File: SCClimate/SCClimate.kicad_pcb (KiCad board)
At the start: 2 copper layers, 100.5 x 54.9 mm, 77 parts, among them J11 HVAC, J3 DISP_SERIAL, J4 SERIAL, J7 PIR, Q1 TEPT5700, Q6 2N6073B, Q7 2N6073B, Q8 2N6073B, SW1 RESET, SW2 MODE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

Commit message: Changed a few things around for better placement
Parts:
- removed SW3: 1825232-1, footprints:1825232-1
- added Q2: 2N7002, digikey-footprints:SOT-23-3, F.Cu at (132.1, 121.9)
- added R3: 10K, Resistor_SMD:R_0805_2012Metric_Pad1.20x1.40mm_HandSolder, F.Cu at (93.3, 92.2)
- added R4: 10K, Resistor_SMD:R_0805_2012Metric_Pad1.20x1.40mm_HandSolder, F.Cu at (128.0, 95.2)
- added R5: 10K, Resistor_SMD:R_0805_2012Metric_Pad1.20x1.40mm_HandSolder, F.Cu at (128.0, 92.3)
- C13, C21, C22, C3, U7: moved to B.Cu
- D2, D3, D4, R12, R15, R16, TRIAC_G1, TRIAC_W1, TRIAC_Y1: moved to F.Cu
- J7: footprint Connector_PinSocket_2.54mm:PinSocket_1x05_P2.54mm_Vertical -> Connector_PinSocket_2.54mm:PinSocket_1x03_P2.54mm_Vertical
- R9: value 20K -> 10K
- moved J11 15.5 mm to (43.1, 96.1), turned to 270 degrees
- moved C22 9.00 mm to (133.7, 95.6), turned to 0 degrees
- moved C21 5.84 mm to (133.7, 93.0), turned to 0 degrees
- moved U7 3.23 mm to (130.8, 87.6), turned to 270 degrees
- moved J7 2.54 mm to (128.7, 132.8)
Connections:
- J11 pad 1: /G_TERM -> /RC_TERM
- J11 pad 2: /RC_TERM -> /W_TERM
- J11 pad 4: /C_TERM -> /G_TERM
- J11 pad 5: /W_TERM -> /C_TERM
- J3 pad 4: +5V -> Net-(J3-Pad4)
- J4 pad 2: Net-(J4-Pad2) -> +3V3
- J4 pad 3: +3V3 -> (no net)
- J7 pad 1: Net-(J7-Pad1) -> GND
- J7 pad 2: GND -> /PIR
- J7 pad 3: /PIR -> +5V
- Q1 pad 1: +3V3 -> Net-(Q1-Pad1)
- U1 pad 10: /TRIAC_W -> /TRIAC_G
- U1 pad 11: Net-(U1-Pad11) -> /DISP_EN
- U1 pad 12: Net-(U1-Pad12) -> (no net)
- U1 pad 13: Net-(U1-Pad13) -> (no net)
- U1 pad 14: Net-(U1-Pad14) -> (no net)
- U1 pad 16: Net-(U1-Pad16) -> (no net)
- U1 pad 17: Net-(U1-Pad17) -> (no net)
- U1 pad 18: Net-(U1-Pad18) -> (no net)
- U1 pad 19: Net-(U1-Pad19) -> (no net)
- U1 pad 20: Net-(U1-Pad20) -> (no net)
- U1 pad 21: Net-(U1-Pad21) -> (no net)
- U1 pad 22: Net-(U1-Pad22) -> (no net)
- U1 pad 23: Net-(U1-Pad23) -> (no net)
- U1 pad 24: Net-(U1-Pad24) -> (no net)
- U1 pad 27: Net-(U1-Pad27) -> (no net)
- U1 pad 28: Net-(U1-Pad28) -> (no net)
- U1 pad 32: Net-(U1-Pad32) -> (no net)
- U1 pad 33: /ESP_GPIO26 -> (no net)
- U1 pad 36: /I2C_SDA -> /I2C_SCL
- U1 pad 37: /I2C_SCL -> /I2C_SDA
- U1 pad 4: Net-(U1-Pad4) -> (no net)
- U1 pad 5: Net-(U1-Pad5) -> (no net)
- U1 pad 7: Net-(U1-Pad7) -> (no net)
- U1 pad 8: /TRIAC_Y -> /TRIAC_W
- U1 pad 9: /TRIAC_G -> /TRIAC_Y
- U10 pad 3: Net-(U10-Pad3) -> (no net)
- U10 pad 5: Net-(U10-Pad5) -> (no net)
- U11 pad 3: Net-(U11-Pad3) -> (no net)
- U11 pad 5: Net-(U11-Pad5) -> (no net)
- U3 pad 3: /EN -> +VDC
- U7 pad 2: Net-(U7-Pad2) -> (no net)
- U7 pad 5: Net-(U7-Pad5) -> +3V3
- U9 pad 3: Net-(U9-Pad3) -> (no net)
- U9 pad 5: Net-(U9-Pad5) -> (no net)
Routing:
- net /DISP_EN: track 0.00 -> 53.2 mm, vias 0 -> 2
- net +VDC: track 77.2 -> 33.4 mm
- net /EN: track 36.4 -> 0.00 mm, vias 1 -> 0
- net +3V3: track 138.9 -> 157.9 mm, vias 1 -> 2
- net GND: track 12.8 -> 27.9 mm, vias 2 -> 4
- net /RC_TERM: track 65.3 -> 77.4 mm
- net /C_TERM: track 28.6 -> 17.3 mm
- net /Y_TERM: track 11.1 -> 18.9 mm
- net /G_TERM: track 12.3 -> 18.0 mm
- net /W_TERM: track 11.8 -> 17.3 mm
- net Net-(Q1-Pad1): track 0.00 -> 4.22 mm
- net /I2C_SCL: track 12.9 -> 16.9 mm, vias 0 -> 1
- net Net-(J3-Pad4): track 0.00 -> 3.78 mm
- net +5V: track 111.0 -> 107.6 mm, vias 2 -> 1
- net /TRIAC_W: track 40.6 -> 43.9 mm, vias 1 -> 2
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
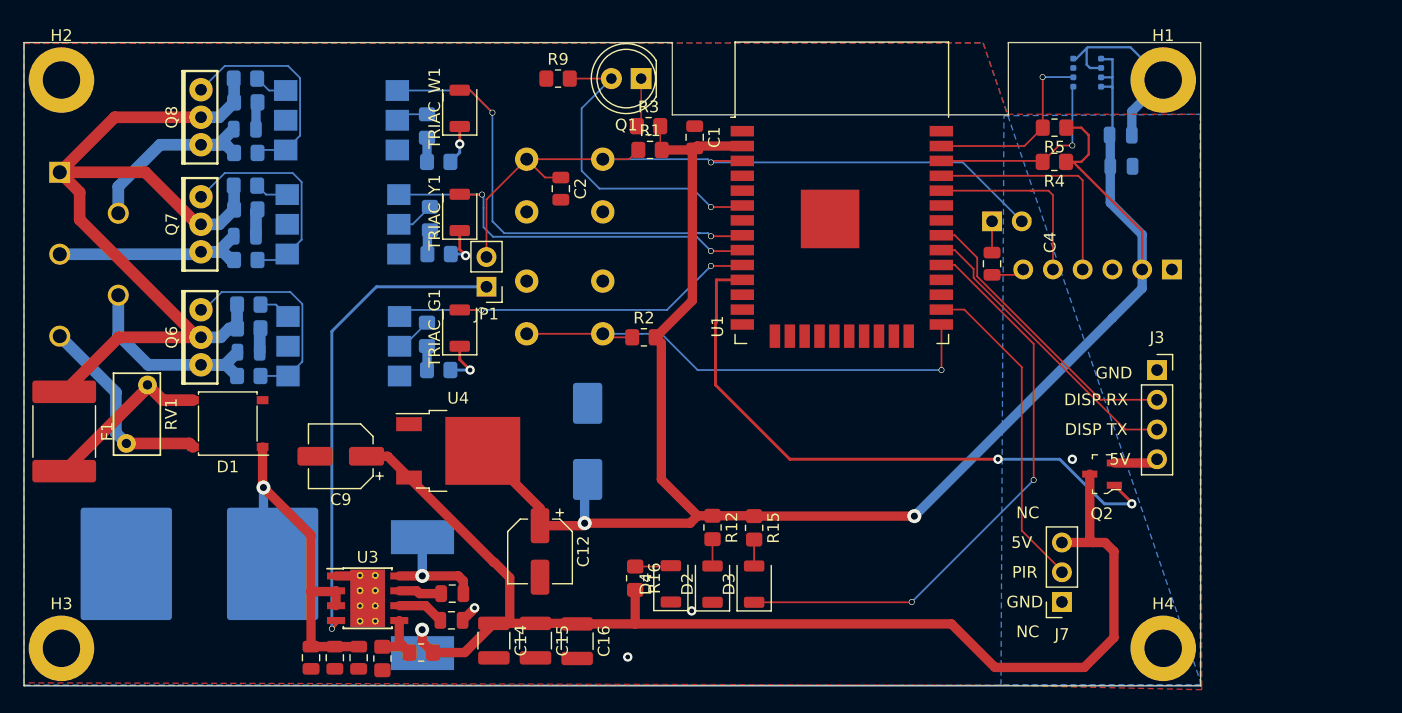
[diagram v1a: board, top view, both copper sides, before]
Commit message: Moved 680 to bottom and switched ldo to buck
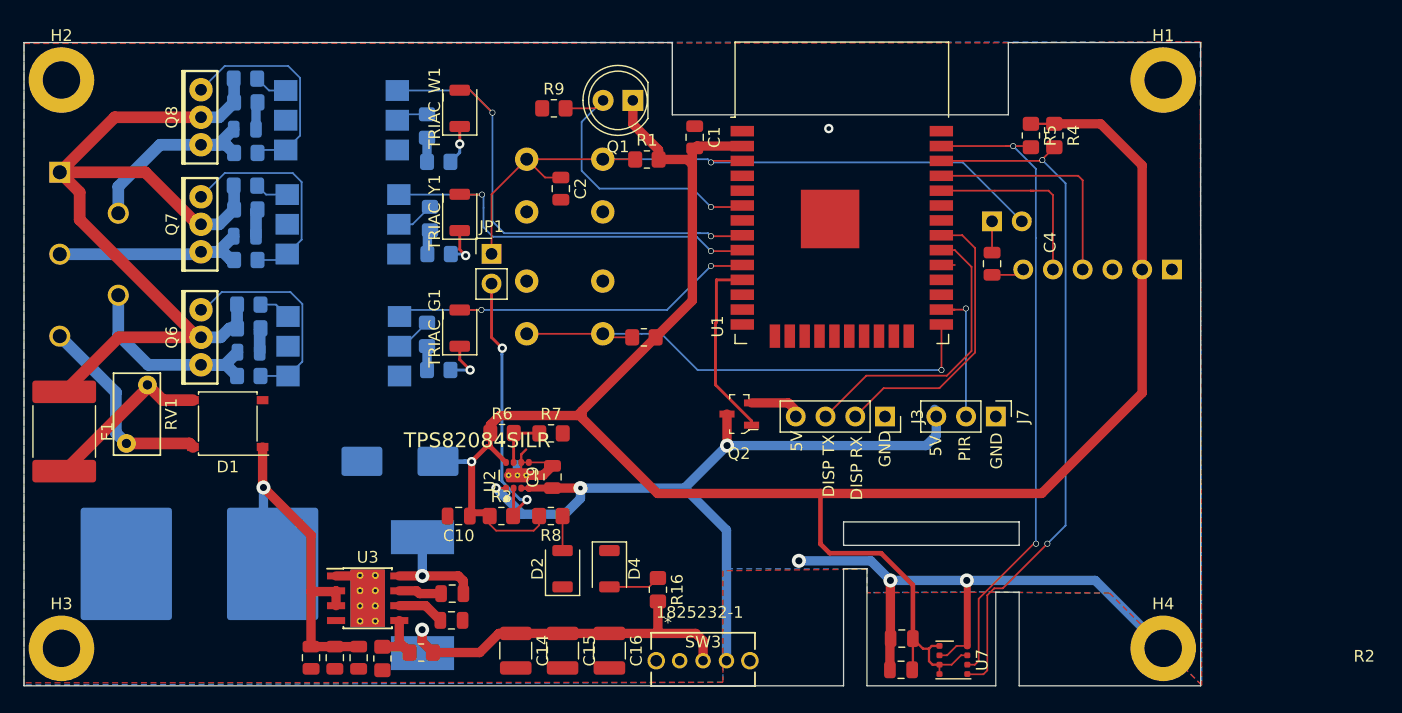
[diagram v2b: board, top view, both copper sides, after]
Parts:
- removed C13: 220 uF, Capacitor_SMD:CP_Elec_8x10
- removed D3: STATUS, LED_SMD:LED_1206_3216Metric_ReverseMount_Hole1.8x2.4mm
- removed R12: 1K6, Resistor_SMD:R_0805_2012Metric_Pad1.20x1.40mm_HandSolder
- removed R15: 120, Resistor_SMD:R_0805_2012Metric_Pad1.20x1.40mm_HandSolder
- removed U4: LD1086DT33TR, Package_TO_SOT_SMD:TO-252-2
- added C10: 10 uF, Capacitor_SMD:C_0805_2012Metric, F.Cu at (77.1, 125.5)
- added R6: 523k, Resistor_SMD:R_0805_2012Metric_Pad1.20x1.40mm_HandSolder, F.Cu at (80.8, 118.4)
- added R7: 169k, Resistor_SMD:R_0805_2012Metric_Pad1.20x1.40mm_HandSolder, F.Cu at (85.0, 118.4)
- added R8: 8K2, Resistor_SMD:R_0805_2012Metric_Pad1.20x1.40mm_HandSolder, F.Cu at (85.0, 125.5)
- added SW3: 1825232-1, footprints:1825232-1, F.Cu at (96.0, 137.9)
- added U2: TPS82084SILR, footprints:Texas_Instruments-SIL0008C-0-0-MFG, F.Cu at (82.1, 122.0)
- C12: value 10 uF -> 220 uF; footprint Capacitor_SMD:CP_Elec_5x5.8 -> Capacitor_SMD:CP_Elec_8x10; moved to B.Cu
- C21, C22, U7: moved to F.Cu
- C9: value 10 uF -> 10 uf; footprint Capacitor_SMD:CP_Elec_5x5.8 -> Capacitor_SMD:C_0805_2012Metric
- D2: value 3V3 -> 3V
- J7: footprint Connector_PinSocket_2.54mm:PinSocket_1x03_P2.54mm_Vertical -> Connector_PinHeader_2.54mm:PinHeader_1x03_P2.54mm_Vertical
- R3: value 10K -> 499k
- R4, R5: value 10K -> 3.3k
- R9: value 10K -> 4K
- moved U7 51.5 mm to (119.4, 137.8)
- moved C22 46.9 mm to (114.9, 138.6), turned to 180 degrees
- moved C21 46.9 mm to (115.0, 136.0), turned to 180 degrees
- moved R3 35.6 mm to (80.8, 125.5)
- moved Q2 31.4 mm to (101.1, 116.8)
- moved J3 23.6 mm to (113.5, 117.0), turned to 270 degrees
- moved C9 18.2 mm to (85.1, 122.2), turned to 90 degrees
- moved J7 16.8 mm to (123.0, 117.0), turned to 270 degrees
- moved C12 14.2 mm to (72.1, 120.8), turned to 180 degrees
- moved D2 12.9 mm to (86.0, 130.0)
- moved D4 5.41 mm to (90.0, 130.0), turned to 270 degrees
- moved C16 2.87 mm to (90.0, 137.0)
- moved JP1 2.84 mm to (79.9, 103.1), turned to 0 degrees
- moved R9 2.56 mm to (85.3, 90.7)
- moved C15 2.47 mm to (86.0, 137.0)
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- renumbered SW2 to MODE, SW1 to RESET
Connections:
- C14 pad 1: +5V -> /5V_Switch
- C15 pad 1: +5V -> /5V_Switch
- C16 pad 1: +5V -> /5V_Switch
- JP1 pad 1: Net-(JP1-Pad1) -> /~ESP_RESET
- JP1 pad 2: /~ESP_RESET -> Net-(JP1-Pad2)
- L1 pad 2: +5V -> /5V_Switch
- Q1 pad 1: Net-(Q1-Pad1) -> +3V3
- R10 pad 1: +5V -> /5V_Switch
- R16 pad 2: +5V -> /5V_Switch
- R3 pad 1: Net-(Q1-Pad1) -> +3V3
- R3 pad 2: +3V3 -> Net-(JP1-Pad2)
- U1 pad 29: /STATUS -> (no net)
- U3 pad 4: Net-(JP1-Pad1) -> (no net)
- U7 pad 2: (no net) -> +3V3
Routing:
- net /STATUS: track 50.5 -> 0.00 mm, vias 2 -> 0
- net /I2C_SCL: track 16.9 -> 59.9 mm, vias 1 -> 2
- net GND: track 27.9 -> 70.1 mm
- net Net-(JP1-Pad1): track 41.7 -> 0.00 mm, vias 1 -> 0
- net /I2C_SDA: track 16.3 -> 56.3 mm, vias 1 -> 2
- net +5V: track 107.6 -> 68.5 mm, vias 1 -> 3
- net /DISP_EN: track 53.2 -> 16.3 mm, vias 2 -> 0
- net /5V_Switch: track 0.00 -> 33.0 mm, vias 0 -> 1
- net +3V3: track 157.9 -> 184.7 mm, vias 2 -> 1
- net Net-(JP1-Pad2): track 0.00 -> 23.8 mm, vias 0 -> 2
- net /PIR: track 27.9 -> 12.5 mm, vias 0 -> 1
- net Net-(R6-Pad2): track 0.00 -> 4.70 mm
- net Net-(Q1-Pad1): track 4.22 -> 0.00 mm
- net Net-(D3-Pad2): track 2.26 -> 0.00 mm
- net /PHOTO: track 27.5 -> 25.3 mm
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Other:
- outline, holes or cut-outs redrawn
- board text added: "5V On/Off"
- board text added: "Pins: 1 RC Terminal 2 W Terminal 3 Y Terminal 4 G Terminal 5 C Terminal"
- board text removed: "Pins: 1 G Terminal 2 RC Terminal 3 Y Terminal 4 C Terminal 5 W Terminal"
- board text removed: "STATUS"

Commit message: Moved 680 to other side of board
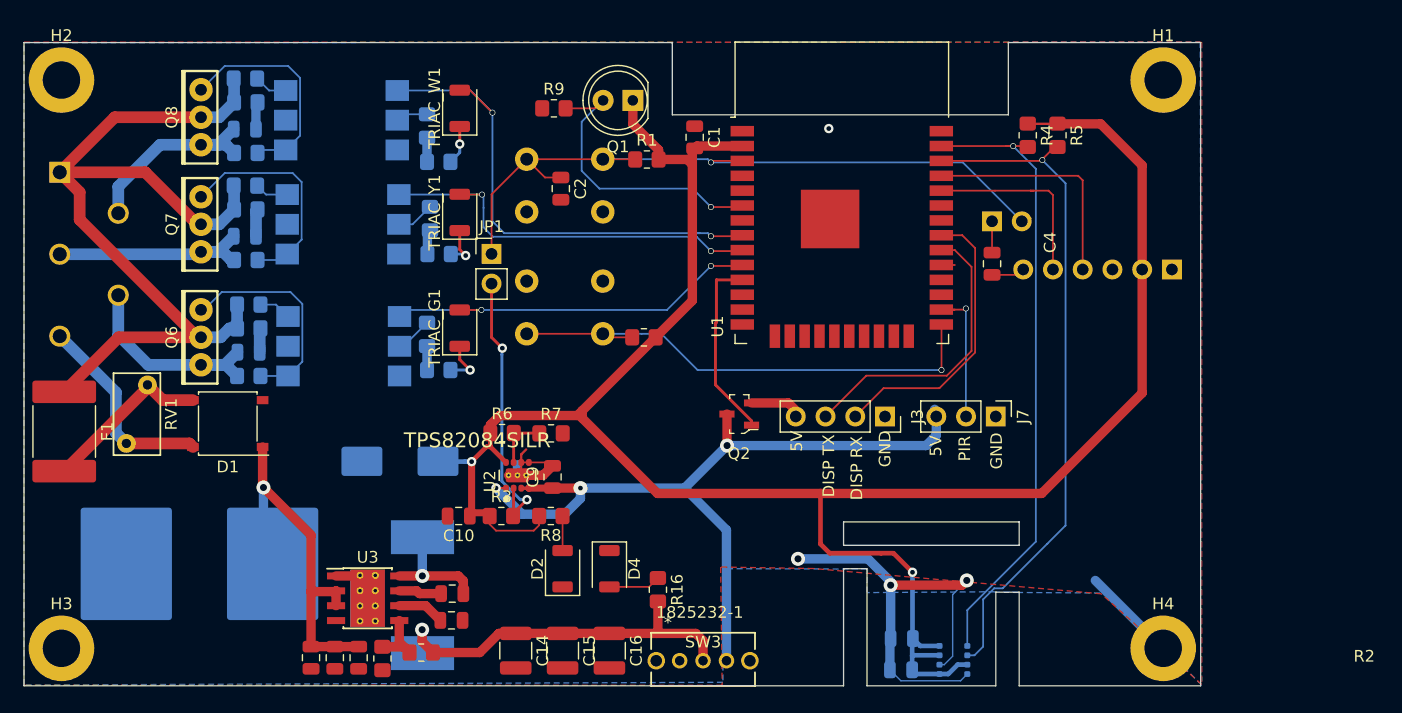
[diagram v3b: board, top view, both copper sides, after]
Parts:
- C21, C22, U7: moved to B.Cu
- moved R5 2.27 mm to (128.3, 93.0)
- moved R4 2.27 mm to (125.7, 93.0)
- turned U7 to 90 degrees
- renumbered RESET to SW1, MODE to SW2
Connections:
- SW3 pad 4: GND -> (no net)
- U1 pad 36: /I2C_SCL -> /I2C_SDA
- U1 pad 37: /I2C_SDA -> /I2C_SCL
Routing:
- net /I2C_SCL: track 59.9 -> 54.2 mm, vias 2 -> 1
- net GND: track 70.1 -> 66.7 mm
- net +3V3: track 184.7 -> 187.1 mm, vias 1 -> 2
- net /I2C_SDA: track 56.3 -> 57.6 mm, vias 2 -> 1
